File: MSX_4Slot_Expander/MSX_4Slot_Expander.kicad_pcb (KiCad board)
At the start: 2 copper layers, 119 x 145.1 mm, 43 parts, among them CN1 MSX_SLOT_CON-msxmakers, CN2 Conn_02x25_Odd_Even_MountingP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, CN3 Conn_02x25_Odd_Even_MountingP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, CN4 Conn_02x25_Odd_Even_MountingP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, CN5 Conn_02x25_Odd_Even_MountingP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, SW1 SW_DIP_x04, U1 74LS30, U2 74LS30, U3 74LS32, U4 74LS240, U5 74LS273, U6 74LS153, U7 74LS139

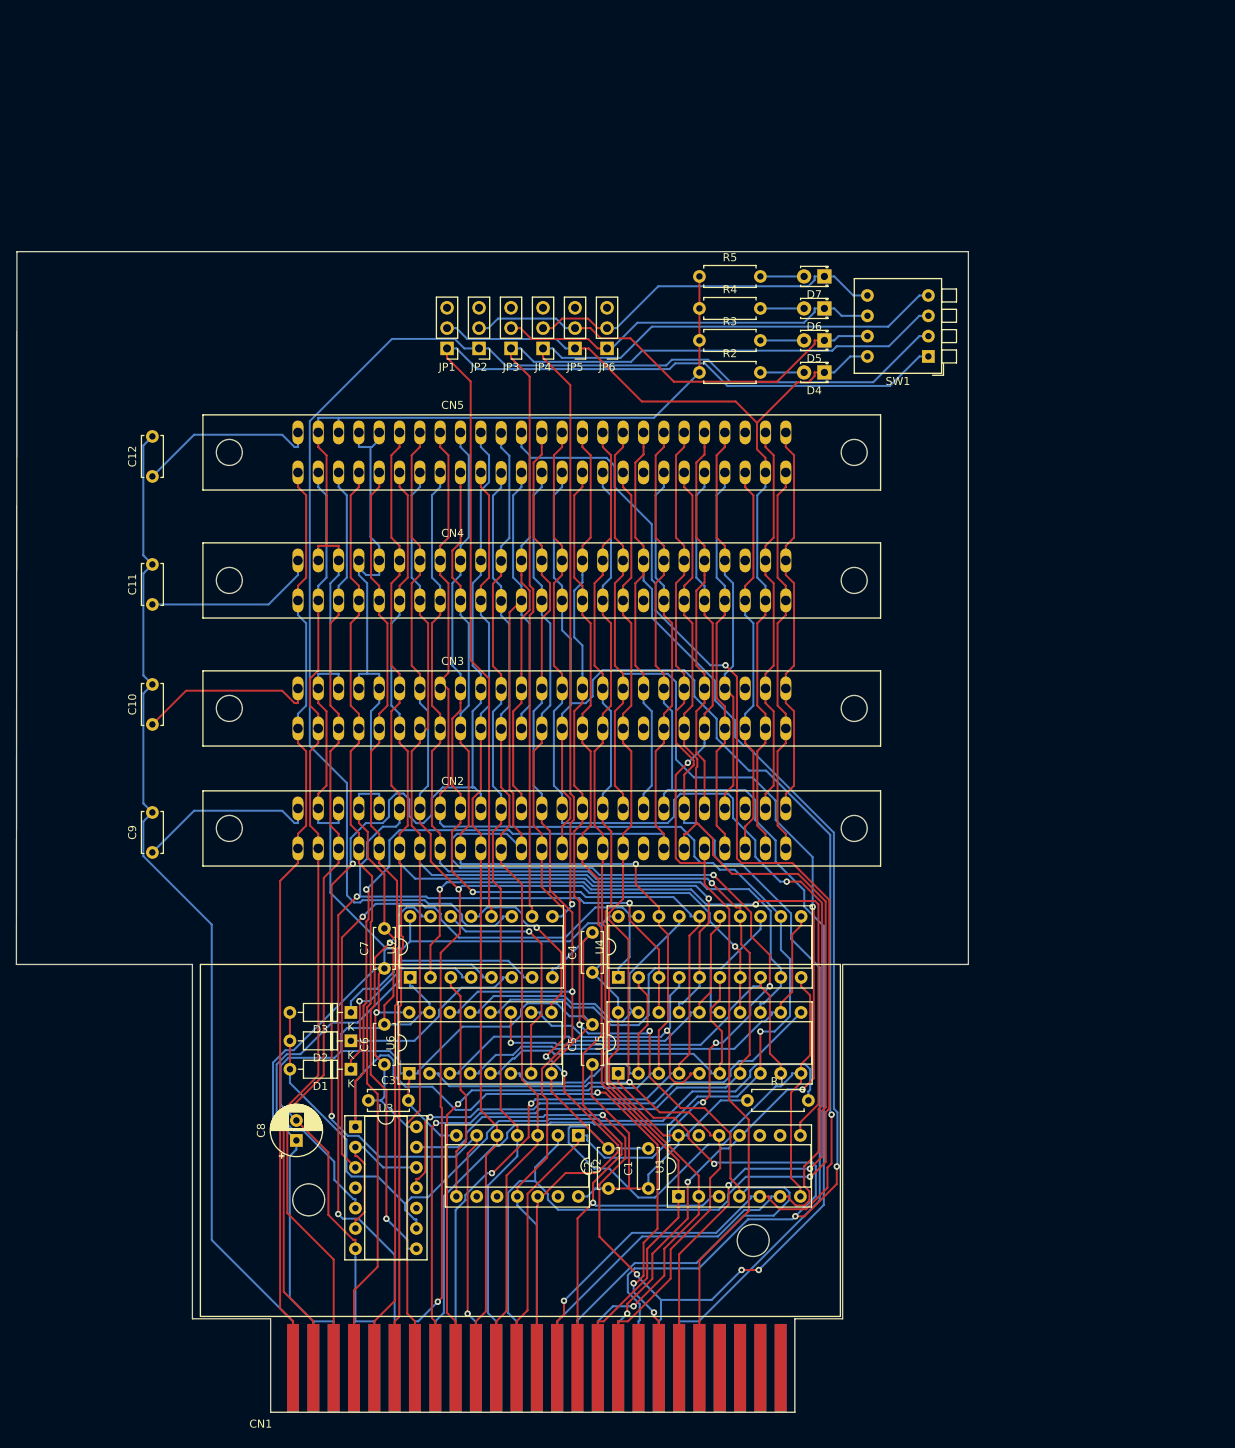
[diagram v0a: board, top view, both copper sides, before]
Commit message: Add files via upload
Added buffers and external +5v supply
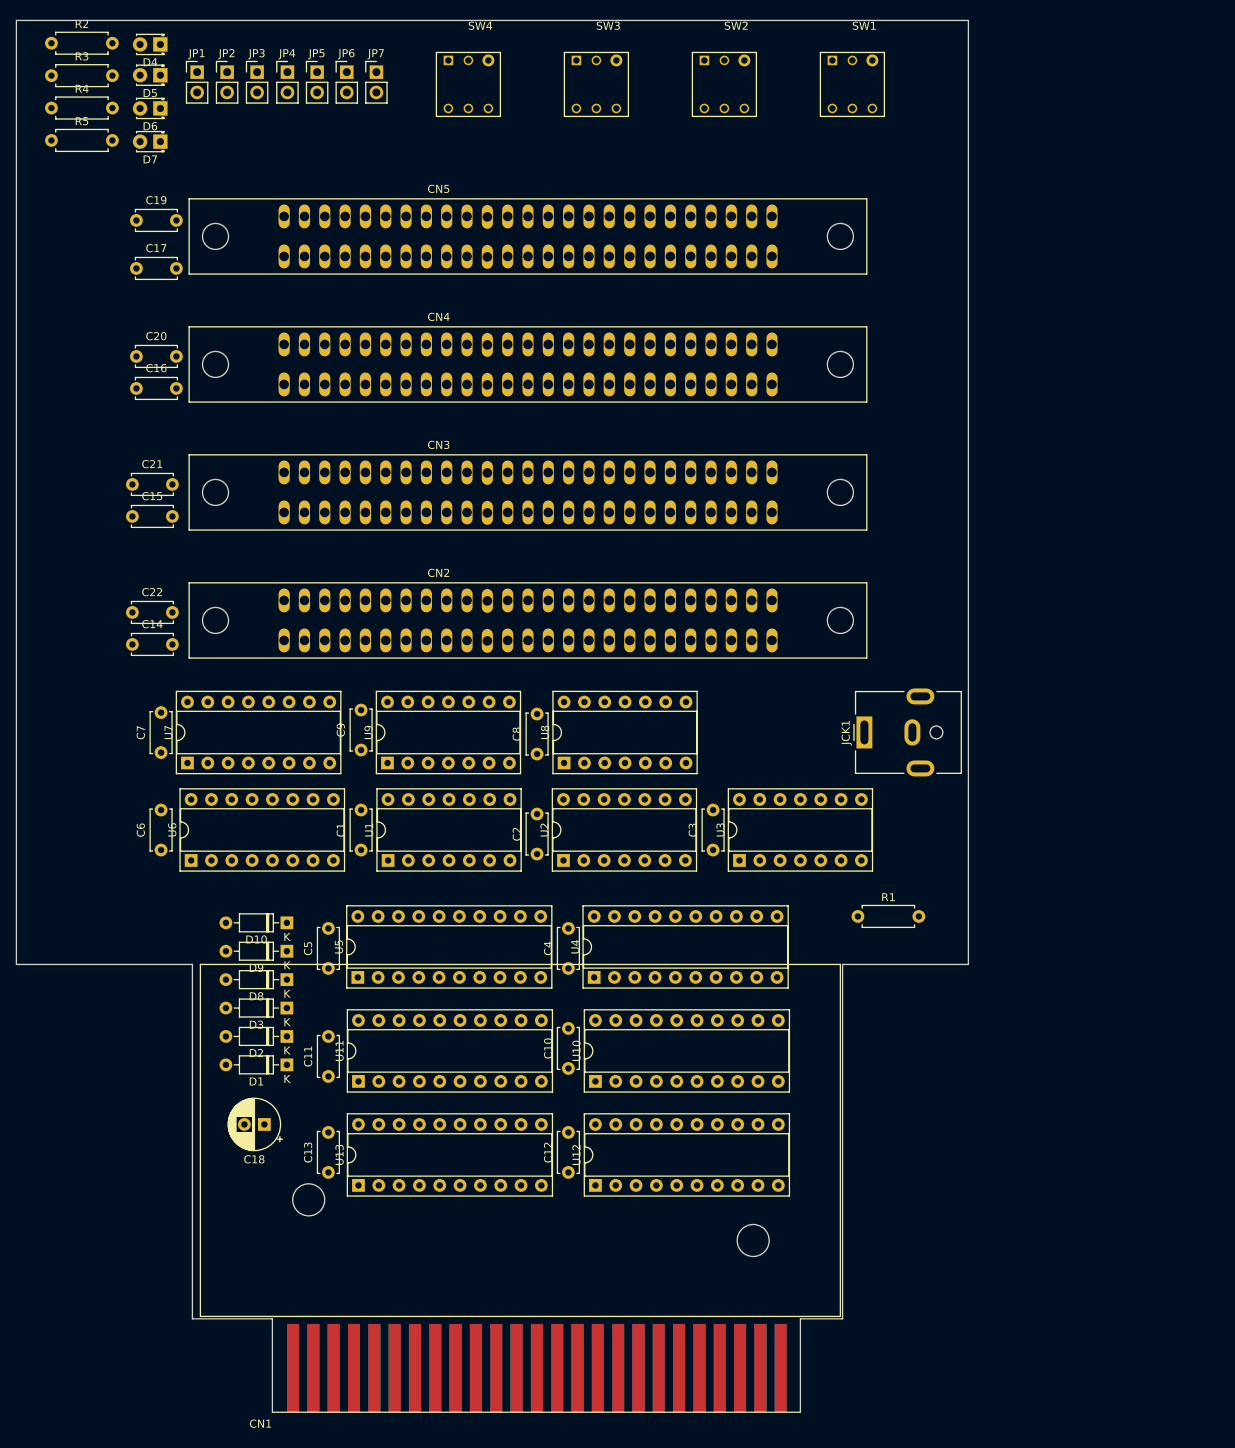
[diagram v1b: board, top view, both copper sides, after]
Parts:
- added C13: 104, Capacitor_THT:C_Disc_D5.0mm_W2.5mm_P5.00mm, F.Cu at (73.0, 194.0)
- added C14: 104, Capacitor_THT:C_Disc_D5.0mm_W2.5mm_P5.00mm, F.Cu at (48.5, 128.0)
- added C15: 104, Capacitor_THT:C_Disc_D5.0mm_W2.5mm_P5.00mm, F.Cu at (48.5, 112.0)
- added C16: 104, Capacitor_THT:C_Disc_D5.0mm_W2.5mm_P5.00mm, F.Cu at (49.0, 96.0)
- added C17: 104, Capacitor_THT:C_Disc_D5.0mm_W2.5mm_P5.00mm, F.Cu at (49.0, 81.0)
- added C18: 100uF, Capacitor_THT:CP_Radial_D6.3mm_P2.50mm, F.Cu at (65.0, 188.0)
- added C19: 104, Capacitor_THT:C_Disc_D5.0mm_W2.5mm_P5.00mm, F.Cu at (49.0, 75.0)
- added C20: 104, Capacitor_THT:C_Disc_D5.0mm_W2.5mm_P5.00mm, F.Cu at (49.0, 92.0)
- added C21: 104, Capacitor_THT:C_Disc_D5.0mm_W2.5mm_P5.00mm, F.Cu at (48.5, 108.0)
- added C22: 104, Capacitor_THT:C_Disc_D5.0mm_W2.5mm_P5.00mm, F.Cu at (48.5, 124.0)
- added D10: 1N914, Diode_THT:D_DO-35_SOD27_P7.62mm_Horizontal, F.Cu at (67.8, 162.8)
- added D8: 1N914, Diode_THT:D_DO-35_SOD27_P7.62mm_Horizontal, F.Cu at (67.8, 169.9)
- added D9: 1N914, Diode_THT:D_DO-35_SOD27_P7.62mm_Horizontal, F.Cu at (67.8, 166.3)
- added JCK1: +5VDC, Connector_BarrelJack:BarrelJack_CUI_PJ-063AH_Horizontal, F.Cu at (140.0, 139.0)
- added JP7: VCC INT, Connector_PinHeader_2.54mm:PinHeader_1x02_P2.54mm_Vertical, F.Cu at (79.0, 56.5)
- added SW2: SW_Push_DPDT, MSX:SW_PUSH_E-Switch_TL2285_DPDT, F.Cu at (120.0, 55.0)
- added SW3: SW_Push_DPDT, MSX:SW_PUSH_E-Switch_TL2285_DPDT, F.Cu at (104.0, 55.0)
- added SW4: SW_Push_DPDT, MSX:SW_PUSH_E-Switch_TL2285_DPDT, F.Cu at (88.0, 55.0)
- added U10: 74HC245, Package_DIP:DIP-20_W7.62mm_Socket, F.Cu at (106.4, 182.6)
- added U11: 74HCT541, Package_DIP:DIP-20_W7.62mm_Socket, F.Cu at (76.8, 182.6)
- added U12: 74HCT541, Package_DIP:DIP-20_W7.62mm_Socket, F.Cu at (106.4, 195.6)
- added U13: 74HCT541, Package_DIP:DIP-20_W7.62mm_Socket, F.Cu at (76.8, 195.6)
- added U8: 74HCT32, Package_DIP:DIP-14_W7.62mm_Socket, F.Cu at (102.5, 142.8)
- added U9: 74LS08, Package_DIP:DIP-14_W7.62mm_Socket, F.Cu at (80.4, 142.8)
- C8: value 100uF -> 104; footprint Capacitor_THT:CP_Radial_D6.3mm_P2.50mm -> Capacitor_THT:C_Disc_D5.0mm_W2.5mm_P5.00mm
- JP1, JP2, JP3, JP4, JP5, JP6: footprint Connector_PinHeader_2.54mm:PinHeader_1x03_P2.54mm_Vertical -> Connector_PinHeader_2.54mm:PinHeader_1x02_P2.54mm_Vertical
- SW1: value SW_DIP_x04 -> SW_Push_DPDT; footprint Button_Switch_THT:SW_DIP_SPSTx04_Piano_10.8x11.72mm_W7.62mm_P2.54mm -> MSX:SW_PUSH_E-Switch_TL2285_DPDT
- moved C12 101.4 mm to (103.0, 194.0)
- moved D4 92.6 mm to (52.0, 53.0)
- moved R2 90.9 mm to (38.4, 52.9)
- moved D5 89.4 mm to (52.0, 56.9)
- moved R3 87.5 mm to (38.4, 56.9)
- moved D6 86.7 mm to (52.0, 61.0)
- moved R4 84.8 mm to (38.4, 61.0)
- moved D7 84.7 mm to (52.0, 65.2)
- moved R5 82.8 mm to (38.4, 65.0)
- moved C10 67.5 mm to (103.0, 181.0)
- moved C11 63.0 mm to (73.0, 182.0)
- moved U3 58.4 mm to (124.4, 155.0), turned to 90 degrees
- moved C8 56.9 mm to (99.1, 141.7)
- moved U1 55.5 mm to (80.5, 155.0)
- moved C1 55.5 mm to (77.1, 153.7)
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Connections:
- net CS1 renamed BXCS1
- net CS12 renamed BXCS12
- net CS2 renamed BXCS2
- net INT renamed BXINT
- net M1 renamed BXM1
- net RFSH renamed BXRFSH
- net SLTLS renamed BXSLTLS
- net WAIT renamed BXWAIT
- C10 pad 1: Net-(CN3-Pin_49) -> +5V
- C10 pad 2: SNDIN -> Earth
- C11 pad 1: Net-(CN4-Pin_49) -> +5V
- C11 pad 2: SNDIN -> Earth
- C12 pad 1: Net-(CN5-Pin_49) -> +5V
- C12 pad 2: SNDIN -> Earth
- C9 pad 1: Net-(CN2-Pin_49) -> +5V
- C9 pad 2: SNDIN -> Earth
- CN2 pad 10: BUSDIR -> BXDIR
- CN2 pad 11: IORQ -> BXIORQ
- CN2 pad 12: MERQ -> BXMERQ
- CN2 pad 13: WR -> BXWR
- CN2 pad 14: RD -> BXRD
- CN2 pad 15: RESET -> BXRESET
- CN2 pad 17: A9 -> BXA9
- CN2 pad 18: A15 -> BXA15
- CN2 pad 19: A11 -> BXA11
- CN2 pad 20: A10 -> BXA10
- CN2 pad 21: A7 -> BXA7
- CN2 pad 22: A6 -> BXA6
- CN2 pad 23: A12 -> BXA12
- CN2 pad 24: A8 -> BXA8
- CN2 pad 25: A14 -> BXA14
- CN2 pad 26: A13 -> BXA13
- CN2 pad 27: A1 -> BXA1
- CN2 pad 28: A0 -> BXA0
- CN2 pad 29: A3 -> BXA3
- CN2 pad 30: A2 -> BXA2
- CN2 pad 31: A5 -> BXA5
- CN2 pad 32: A4 -> BXA4
- CN2 pad 33: D1 -> BXD1
- CN2 pad 34: D0 -> BXD0
- CN2 pad 35: D3 -> BXD3
- CN2 pad 36: D2 -> BXD2
- CN2 pad 37: D5 -> BXD5
- CN2 pad 38: D4 -> BXD4
- CN2 pad 39: D7 -> BXD7
- CN2 pad 40: D6 -> BXD6
- CN2 pad 42: CLK -> BXCLK
- CN2 pad 44: SW1 -> SW10
- CN2 pad 45: +5V -> +5VS0
- CN2 pad 46: SW2 -> SW20
- CN2 pad 47: +5V -> +5VS0
- CN3 pad 10: BUSDIR -> BXDIR
- CN3 pad 11: IORQ -> BXIORQ
- CN3 pad 12: MERQ -> BXMERQ
- CN3 pad 13: WR -> BXWR
- CN3 pad 14: RD -> BXRD
- CN3 pad 15: RESET -> BXRESET
- CN3 pad 17: A9 -> BXA9
- CN3 pad 18: A15 -> BXA15
- CN3 pad 19: A11 -> BXA11
- CN3 pad 20: A10 -> BXA10
- CN3 pad 21: A7 -> BXA7
- CN3 pad 22: A6 -> BXA6
- CN3 pad 23: A12 -> BXA12
- CN3 pad 24: A8 -> BXA8
- CN3 pad 25: A14 -> BXA14
- CN3 pad 26: A13 -> BXA13
- CN3 pad 27: A1 -> BXA1
- CN3 pad 28: A0 -> BXA0
- CN3 pad 29: A3 -> BXA3
- CN3 pad 30: A2 -> BXA2
- CN3 pad 31: A5 -> BXA5
- CN3 pad 32: A4 -> BXA4
- CN3 pad 33: D1 -> BXD1
- CN3 pad 34: D0 -> BXD0
- CN3 pad 35: D3 -> BXD3
- CN3 pad 36: D2 -> BXD2
- CN3 pad 37: D5 -> BXD5
- CN3 pad 38: D4 -> BXD4
- CN3 pad 39: D7 -> BXD7
- CN3 pad 4: SLTX0 -> SLTX1
- CN3 pad 40: D6 -> BXD6
- CN3 pad 42: CLK -> BXCLK
- CN3 pad 44: SW1 -> SW11
- CN3 pad 45: +5V -> +5VS1
- CN3 pad 46: SW2 -> SW21
- CN3 pad 47: +5V -> +5VS1
- CN4 pad 10: BUSDIR -> BXDIR
- CN4 pad 11: IORQ -> BXIORQ
- CN4 pad 12: MERQ -> BXMERQ
- CN4 pad 13: WR -> BXWR
- CN4 pad 14: RD -> BXRD
- CN4 pad 15: RESET -> BXRESET
- CN4 pad 17: A9 -> BXA9
- CN4 pad 18: A15 -> BXA15
- CN4 pad 19: A11 -> BXA11
- CN4 pad 20: A10 -> BXA10
- CN4 pad 21: A7 -> BXA7
- CN4 pad 22: A6 -> BXA6
- CN4 pad 23: A12 -> BXA12
- CN4 pad 24: A8 -> BXA8
- CN4 pad 25: A14 -> BXA14
- CN4 pad 26: A13 -> BXA13
- CN4 pad 27: A1 -> BXA1
- CN4 pad 28: A0 -> BXA0
- CN4 pad 29: A3 -> BXA3
- CN4 pad 30: A2 -> BXA2
- CN4 pad 31: A5 -> BXA5
- CN4 pad 32: A4 -> BXA4
- CN4 pad 33: D1 -> BXD1
- CN4 pad 34: D0 -> BXD0
- CN4 pad 35: D3 -> BXD3
- CN4 pad 36: D2 -> BXD2
- CN4 pad 37: D5 -> BXD5
- CN4 pad 38: D4 -> BXD4
- CN4 pad 39: D7 -> BXD7
- CN4 pad 4: SLTX0 -> SLTX2
- CN4 pad 40: D6 -> BXD6
- CN4 pad 42: CLK -> BXCLK
- CN4 pad 44: SW1 -> SW12
- CN4 pad 45: +5V -> +5VS2
- CN4 pad 46: SW2 -> SW22
- CN4 pad 47: +5V -> +5VS2
- CN5 pad 10: BUSDIR -> BXDIR
- CN5 pad 11: IORQ -> BXIORQ
- CN5 pad 12: MERQ -> BXMERQ
- CN5 pad 13: WR -> BXWR
- CN5 pad 14: RD -> BXRD
- CN5 pad 15: RESET -> BXRESET
- CN5 pad 17: A9 -> BXA9
- CN5 pad 18: A15 -> BXA15
- CN5 pad 19: A11 -> BXA11
- CN5 pad 20: A10 -> BXA10
- CN5 pad 21: A7 -> BXA7
- CN5 pad 22: A6 -> BXA6
- CN5 pad 23: A12 -> BXA12
- CN5 pad 24: A8 -> BXA8
- CN5 pad 25: A14 -> BXA14
- CN5 pad 26: A13 -> BXA13
- CN5 pad 27: A1 -> BXA1
- CN5 pad 28: A0 -> BXA0
- CN5 pad 29: A3 -> BXA3
- CN5 pad 30: A2 -> BXA2
- CN5 pad 31: A5 -> BXA5
- CN5 pad 32: A4 -> BXA4
- CN5 pad 33: D1 -> BXD1
- CN5 pad 34: D0 -> BXD0
- CN5 pad 35: D3 -> BXD3
- CN5 pad 36: D2 -> BXD2
- CN5 pad 37: D5 -> BXD5
- CN5 pad 38: D4 -> BXD4
- CN5 pad 39: D7 -> BXD7
- CN5 pad 4: SLTX0 -> SLTX3
- CN5 pad 40: D6 -> BXD6
- CN5 pad 42: CLK -> BXCLK
- CN5 pad 44: SW1 -> SW13
- CN5 pad 45: +5V -> +5VS3
- CN5 pad 46: SW2 -> SW23
- CN5 pad 47: +5V -> +5VS3
- JP1 pad 2: SLTX0 -> Net-(JP1-B)
- JP2 pad 2: SLTX1 -> Net-(JP2-B)
- JP3 pad 2: SLTX2 -> Net-(JP3-B)
- JP4 pad 2: SLTX3 -> Net-(JP4-B)
- JP5 pad 1: SLTX0 -> Net-(JP1-B)
- JP5 pad 2: SLTX1 -> Net-(JP2-B)
- JP6 pad 1: SLTX2 -> Net-(JP3-B)
- JP6 pad 2: SLTX3 -> Net-(JP4-B)
- SW1 pad 1: Net-(JP1-A) -> unconnected-(SW1-A-Pad1)
- SW1 pad 2: Net-(JP2-A) -> Net-(JP1-A)
- SW1 pad 3: Net-(JP3-A) -> SLTX0
- SW1 pad 4: Net-(JP4-A) -> unconnected-(SW1-A-Pad4)
- SW1 pad 5: SLTX3 -> +5VS
- SW1 pad 6: SLTX2 -> +5VS0
- U1 pad 1: A10 -> BXA10
- U1 pad 11: A9 -> BXA9
- U1 pad 12: A15 -> BXA15
- U1 pad 2: A11 -> BXA11
- U1 pad 3: A6 -> BXA6
- U1 pad 4: A7 -> BXA7
- U1 pad 5: A8 -> BXA8
- U1 pad 6: A12 -> BXA12
- U2 pad 1: A0 -> BXA0
- U2 pad 11: A14 -> BXA14
- U2 pad 12: A13 -> BXA13
- U2 pad 2: A1 -> BXA1
- U2 pad 3: A2 -> BXA2
- U2 pad 4: A3 -> BXA3
- U2 pad 5: A4 -> BXA4
- U2 pad 6: A5 -> BXA5
- U3 pad 1: RD -> BXRD
- U3 pad 13: WR -> BXWR
- U3 pad 4: SLTSL -> BXSLTSL
- U4 pad 12: D3 -> BXD3
- U4 pad 14: D2 -> BXD2
- U4 pad 16: D1 -> BXD1
- U4 pad 18: D0 -> BXD0
- U4 pad 3: D7 -> BXD7
- U4 pad 5: D6 -> BXD6
- U4 pad 7: D5 -> BXD5
- U4 pad 9: D4 -> BXD4
- U5 pad 1: RESET -> BXRESET
- U5 pad 13: D4 -> BXD4
- U5 pad 14: D5 -> BXD5
- U5 pad 17: D6 -> BXD6
- U5 pad 18: D7 -> BXD7
- U5 pad 3: D0 -> BXD0
- U5 pad 4: D1 -> BXD1
- U5 pad 7: D2 -> BXD2
- U5 pad 8: D3 -> BXD3
- U6 pad 14: A14 -> BXA14
- U6 pad 2: A15 -> BXA15
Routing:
- net +5V: track 360.3 -> 0.00 mm, vias 1 -> 0
- net Earth: track 346.0 -> 0.00 mm
- net A1: track 238.1 -> 0.00 mm, vias 2 -> 0
- net RESET: track 219.0 -> 0.00 mm, vias 3 -> 0
- net RD: track 207.2 -> 0.00 mm, vias 4 -> 0
- net WR: track 203.0 -> 0.00 mm, vias 4 -> 0
- net A0: track 199.9 -> 0.00 mm, vias 4 -> 0
- net D3: track 192.0 -> 0.00 mm, vias 1 -> 0
- net A8: track 189.6 -> 0.00 mm, vias 2 -> 0
- net D2: track 184.5 -> 0.00 mm, vias 2 -> 0
- net D4: track 179.1 -> 0.00 mm
- net A12: track 178.1 -> 0.00 mm, vias 1 -> 0
- net D7: track 177.2 -> 0.00 mm, vias 3 -> 0
- net D6: track 173.4 -> 0.00 mm, vias 1 -> 0
- net Net-(JP2-A): track 171.5 -> 0.00 mm
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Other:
- board size 119 x 145.1 mm -> 119 x 174 mm

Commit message: Add files via upload
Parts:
- removed SW4: SW_Push_DPDT, MSX:SW_PUSH_E-Switch_TL2285_DPDT
- added C14: 104, Capacitor_THT:C_Disc_D5.0mm_W2.5mm_P5.00mm, F.Cu at (108.0, 142.1)
- added C15: 104, Capacitor_THT:C_Disc_D5.0mm_W2.5mm_P5.00mm, F.Cu at (131.0, 142.0)
- added C16: 104, Capacitor_THT:C_Disc_D5.0mm_W2.5mm_P5.00mm, F.Cu at (131.5, 154.0)
- added C22: 100uF, Capacitor_THT:CP_Radial_D6.3mm_P2.50mm, F.Cu at (147.0, 160.5)
- added PS1: IH0512D, Converter_DCDC:Converter_DCDC_XP_POWER-IHxxxxD_THT, F.Cu at (169.4, 134.3)
- added SW5: SW_Push_4PDT, MSX:Push Switch 4P2T SPUJ193700, F.Cu at (167.5, 112.5)
- added U11: 74LS11, Package_DIP:DIP-14_W7.62mm_Socket, F.Cu at (134.3, 155.6)
- added U12: 74LS08, Package_DIP:DIP-14_W7.62mm_Socket, F.Cu at (134.4, 142.8)
- added U13: 74LS32, Package_DIP:DIP-14_W7.62mm_Socket, F.Cu at (111.3, 142.6)
- added U17: AQH0223, Package_DIP:DIP-8-N7_W7.62mm, F.Cu at (156.4, 163.8)
- added U18: AQH0223, Package_DIP:DIP-8-N7_W7.62mm, F.Cu at (156.4, 153.0)
- added U19: AQH0223, Package_DIP:DIP-8-N7_W7.62mm, F.Cu at (156.4, 142.2)
- SW1, SW2, SW3: value SW_Push_DPDT -> SW_Push_4PDT; footprint MSX:SW_PUSH_E-Switch_TL2285_DPDT -> MSX:Push Switch 4P2T SPUJ193700
- moved D7 135.0 mm to (179.5, 109.5)
- moved D6 131.8 mm to (179.5, 94.5)
- moved D5 129.3 mm to (179.5, 78.5)
- moved D4 127.9 mm to (179.5, 62.5)
- moved R5 119.2 mm to (144.5, 119.3), turned to 90 degrees
- moved JP6 118.7 mm to (173.3, 123.5)
- moved JP1 118.7 mm to (154.6, 123.5)
- moved JP2 118.7 mm to (158.3, 123.5)
- moved JP3 118.7 mm to (162.1, 123.5)
- moved JP4 118.7 mm to (165.9, 123.5)
- moved JP5 118.7 mm to (169.6, 123.5)
- moved JP7 118.7 mm to (177.0, 123.5)
- moved R4 114.3 mm to (144.5, 103.5), turned to 90 degrees
- moved R3 110.4 mm to (144.5, 87.5), turned to 90 degrees
- moved R2 107.7 mm to (144.5, 71.3), turned to 90 degrees
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- renumbered C14 to C17, C15 to C18, C16 to C19, C17 to C20, C18 to C21, U10 to U1, U3 to U10, U5 to U14, U4 to U15, U6 to U16, U11 to U2, U12 to U3, U13 to U4, U9 to U5, U8 to U6, U1 to U7, U2 to U8, U7 to U9
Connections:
- C10 pad 1: +5V -> +5VS
- C11 pad 1: +5V -> +5VS
- C12 pad 1: +5V -> +5VS
- C13 pad 1: +5V -> +5VS
- C21 pad 1: +5V -> +5VS
- C7 pad 1: +5V -> +5VS
- C8 pad 1: +5V -> +5VS
- C9 pad 1: +5V -> +5VS
- CN2 pad 10: BXDIR -> BXDIR0
- CN2 pad 48: +12V -> +12VS0
- CN2 pad 50: -12V -> -12VS0
- CN3 pad 10: BXDIR -> BXDIR1
- CN3 pad 48: +12V -> +12VS1
- CN3 pad 50: -12V -> -12VS1
- CN4 pad 10: BXDIR -> BXDIR2
- CN4 pad 48: +12V -> +12VS2
- CN4 pad 50: -12V -> -12VS2
- CN5 pad 10: BXDIR -> BXDIR3
- CN5 pad 48: +12V -> +12VS3
- CN5 pad 50: -12V -> -12VS3
- JCK1 pad 1: +5VS -> Net-(PS1-+Vin)
- R2 pad 1: +5V -> +5VS
- R3 pad 1: +5V -> +5VS
- R4 pad 1: +5V -> +5VS
- R5 pad 1: +5V -> +5VS
- SW1 pad 1: unconnected-(SW1-A-Pad1) -> SLTX1
- SW1 pad 2: Net-(JP1-A) -> Net-(JP2-A)
- SW1 pad 3: SLTX0 -> unconnected-(SW1-C-Pad3)
- SW1 pad 6: +5VS0 -> +5VS1
- SW2 pad 1: unconnected-(SW2-A-Pad1) -> SLTX2
- SW2 pad 2: Net-(JP2-A) -> Net-(JP3-A)
- SW2 pad 3: SLTX1 -> unconnected-(SW2-C-Pad3)
- SW2 pad 6: +5VS1 -> +5VS2
- SW3 pad 1: unconnected-(SW3-A-Pad1) -> SLTX3
- SW3 pad 2: Net-(JP3-A) -> Net-(JP4-A)
- SW3 pad 3: SLTX2 -> unconnected-(SW3-C-Pad3)
- SW3 pad 6: +5VS2 -> +5VS3
- U10 pad 14: +5V -> +5VS
- U10 pad 9: Net-(D1-A) -> Net-(U10-Pad9)
- U14 pad 20: +5V -> +5VS
- U15 pad 20: +5V -> +5VS
- U16 pad 16: +5V -> +5VS
- U7 pad 14: +5V -> +5VS
- U8 pad 14: +5V -> +5VS
- U9 pad 16: +5V -> +5VS
- U9 pad 5: Net-(D1-K) -> Net-(U9A-O1)
- U9 pad 6: Net-(D2-K) -> Net-(U9A-O2)
- U9 pad 7: Net-(D3-K) -> Net-(U9A-O3)
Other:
- board size 119 x 174 mm -> 149 x 167 mm
